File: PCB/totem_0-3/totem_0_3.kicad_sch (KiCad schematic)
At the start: 88 parts, among them J1 MJ-4PP-9, J2 MJ-4PP-9, U1 xiao-ble, U2 xiao-ble

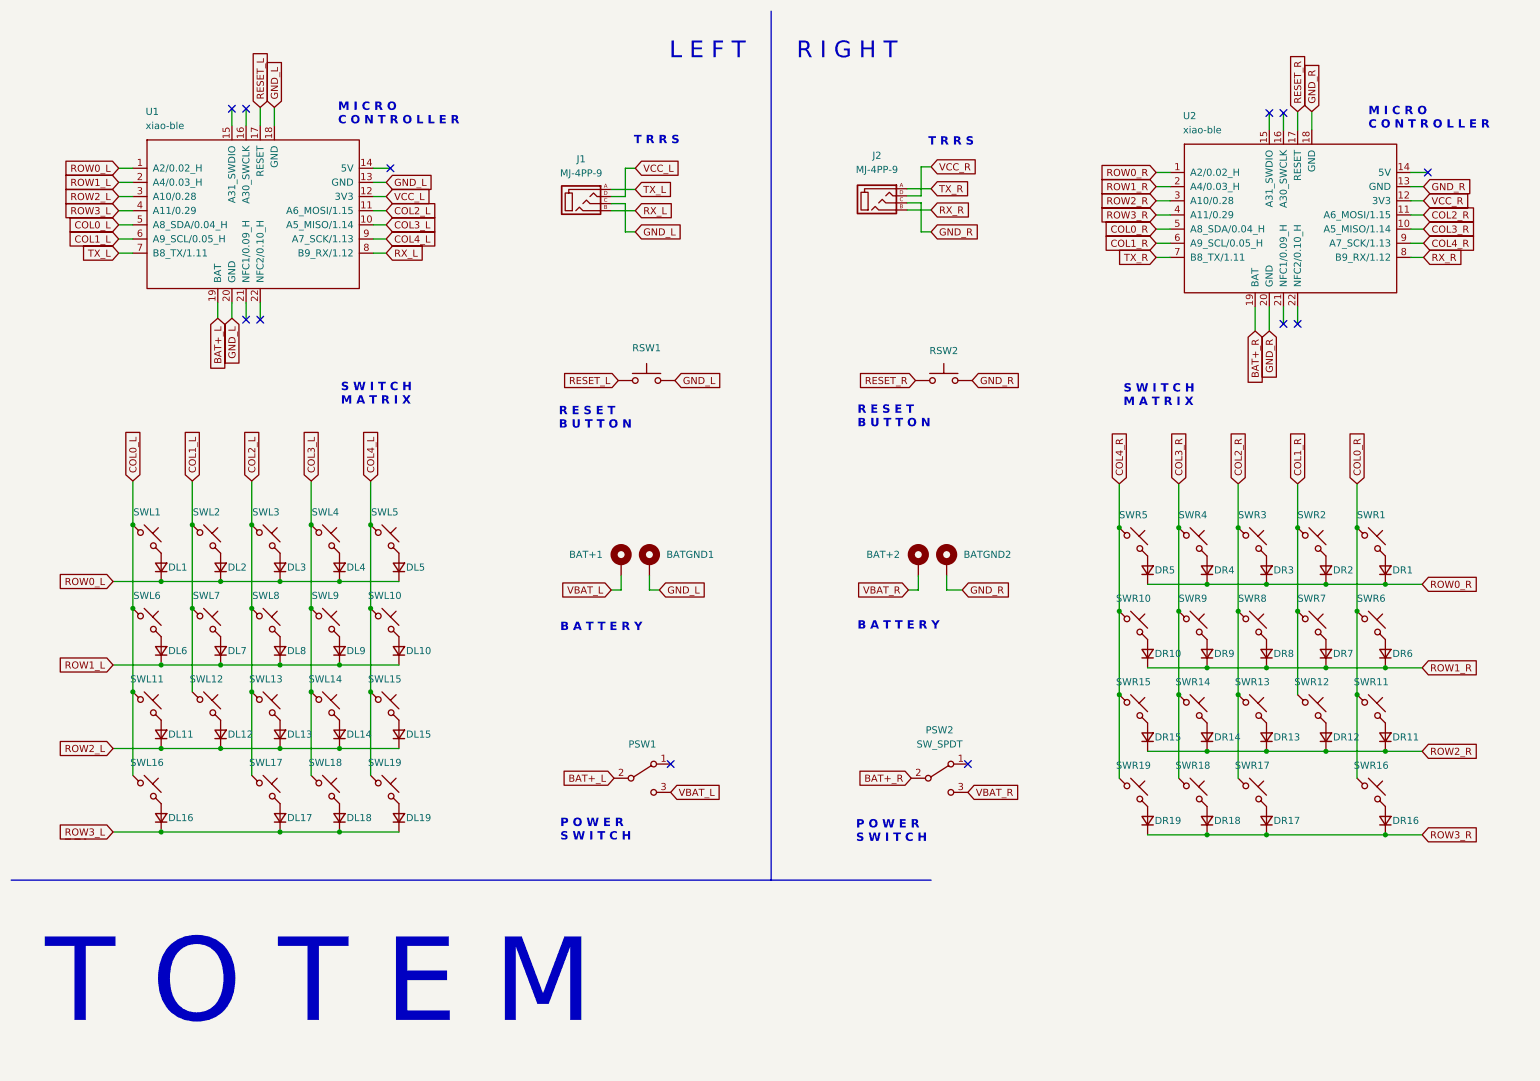
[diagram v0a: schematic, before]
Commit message: feat(board): change pin connections
basically remove UART and add I2C
move GPIO around to get the needed pins

Pin 5: COL0 -> SDA
Pin 6: COL1 -> SCL
Pin 7: TX -> RDY
Pin 8: RX -> X
Pin 15: X -> COL1
Pin 16: X -> COL0
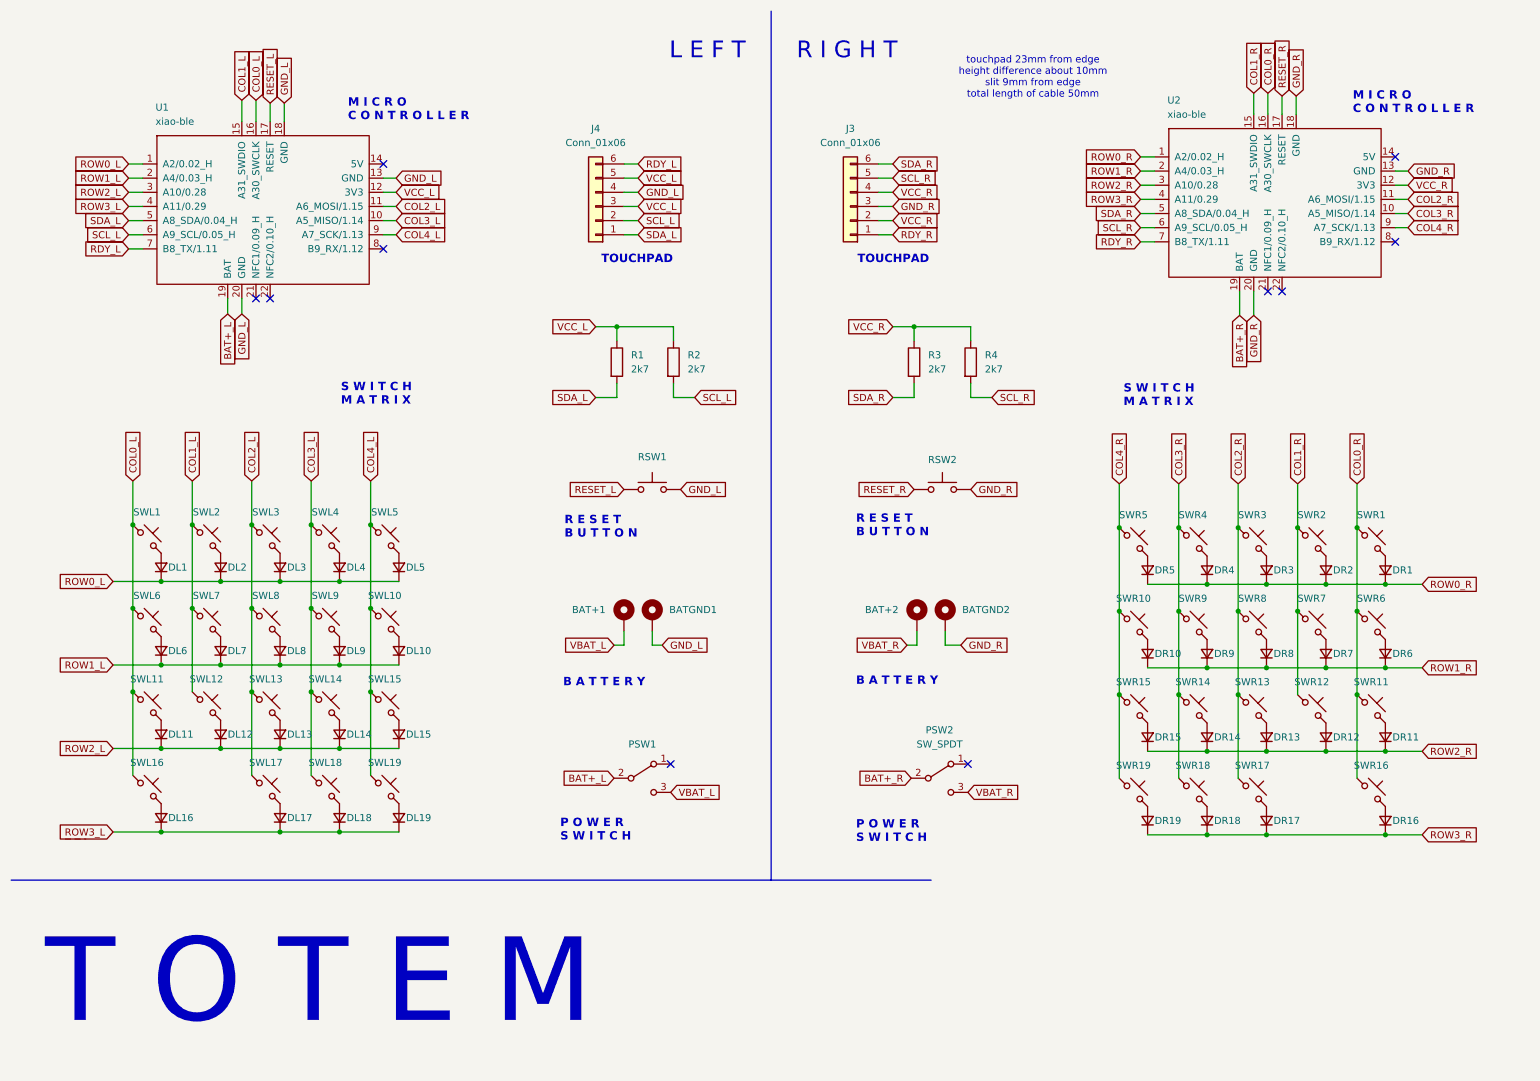
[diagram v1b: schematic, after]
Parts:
- removed J1, J2: MJ-4PP-9, TOTEMlib:MJ-4PP-9_1side, symbol kbd:MJ-4PP-9
- added J3, J4: Conn_01x06, Connector_FFC-FPC:TE_0-1734839-6_1x06-1MP_P0.5mm_Horizontal, symbol Connector_Generic:Conn_01x06
- added R1, R2, R3, R4: 2k7, Resistor_SMD:R_0603_1608Metric_Pad0.98x0.95mm_HandSolder, symbol Device:R
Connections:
- net COL0_L: now also U1.16 (A30_SWCLK); no longer U1.5 (A8_SDA/0.04_H)
- net COL0_R: now also U2.16 (A30_SWCLK); no longer U2.5 (A8_SDA/0.04_H)
- net COL1_L: now also U1.15 (A31_SWDIO); no longer U1.6 (A9_SCL/0.05_H)
- net COL1_R: now also U2.15 (A31_SWDIO); no longer U2.6 (A9_SCL/0.05_H)
- net GND_L: now also J4.4 (Pin_4)
- net GND_R: now also J3.3 (Pin_3)
- net VCC_L: now also J4.3 (Pin_3), J4.5 (Pin_5), R1.1, R2.1
- net VCC_R: now also J3.2 (Pin_2), J3.4 (Pin_4), R3.1, R4.1
- net RX_L: no longer names the net of U1.8 (B9_RX/1.12)
- net RX_R: no longer names the net of U2.8 (B9_RX/1.12)
- net TX_L renamed RDY_L
- net RDY_L: now also J4.6 (Pin_6)
- net TX_R renamed RDY_R
- net RDY_R: now also J3.1 (Pin_1)
- new net SCL_L: J4.2 (Pin_2), R2.2, U1.6 (A9_SCL/0.05_H)
- new net SCL_R: J3.5 (Pin_5), R4.2, U2.6 (A9_SCL/0.05_H)
- new net SDA_L: J4.1 (Pin_1), R1.2, U1.5 (A8_SDA/0.04_H)
- new net SDA_R: J3.6 (Pin_6), R3.2, U2.5 (A8_SDA/0.04_H)
- no-connect marks 12 -> 10
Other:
- note added: "TOUCHPAD"
- note added: "touchpad 23mm from edge height difference about 10mm slit 9mm from edge total length of cable 50mm"
- note removed: "T R R S"
- moved on the sheet: BAT+1, BAT+2, BATGND1, BATGND2, RSW1, RSW2, U1, U2
